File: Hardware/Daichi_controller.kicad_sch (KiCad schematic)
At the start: 24 parts, among them J1 USB_B_Mini, J2 S21, Q1 BF545A

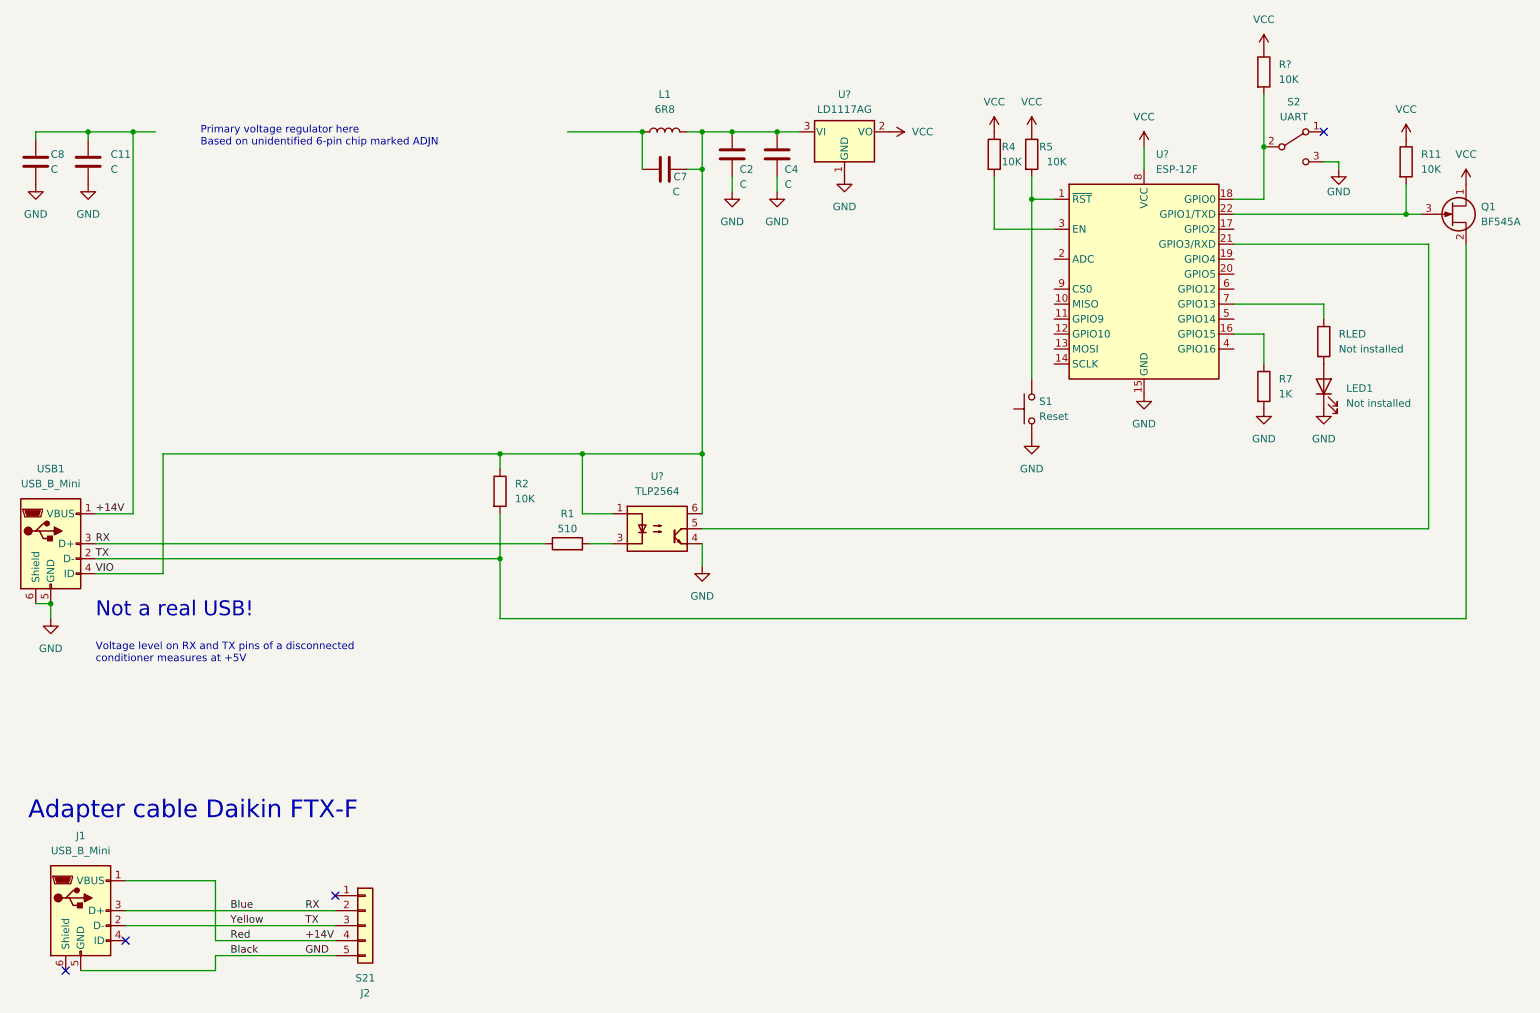
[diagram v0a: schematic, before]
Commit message: Hardware: Fix reference schematic
Q1 was drawn incorrectly. Thanks @glinka65 for hints
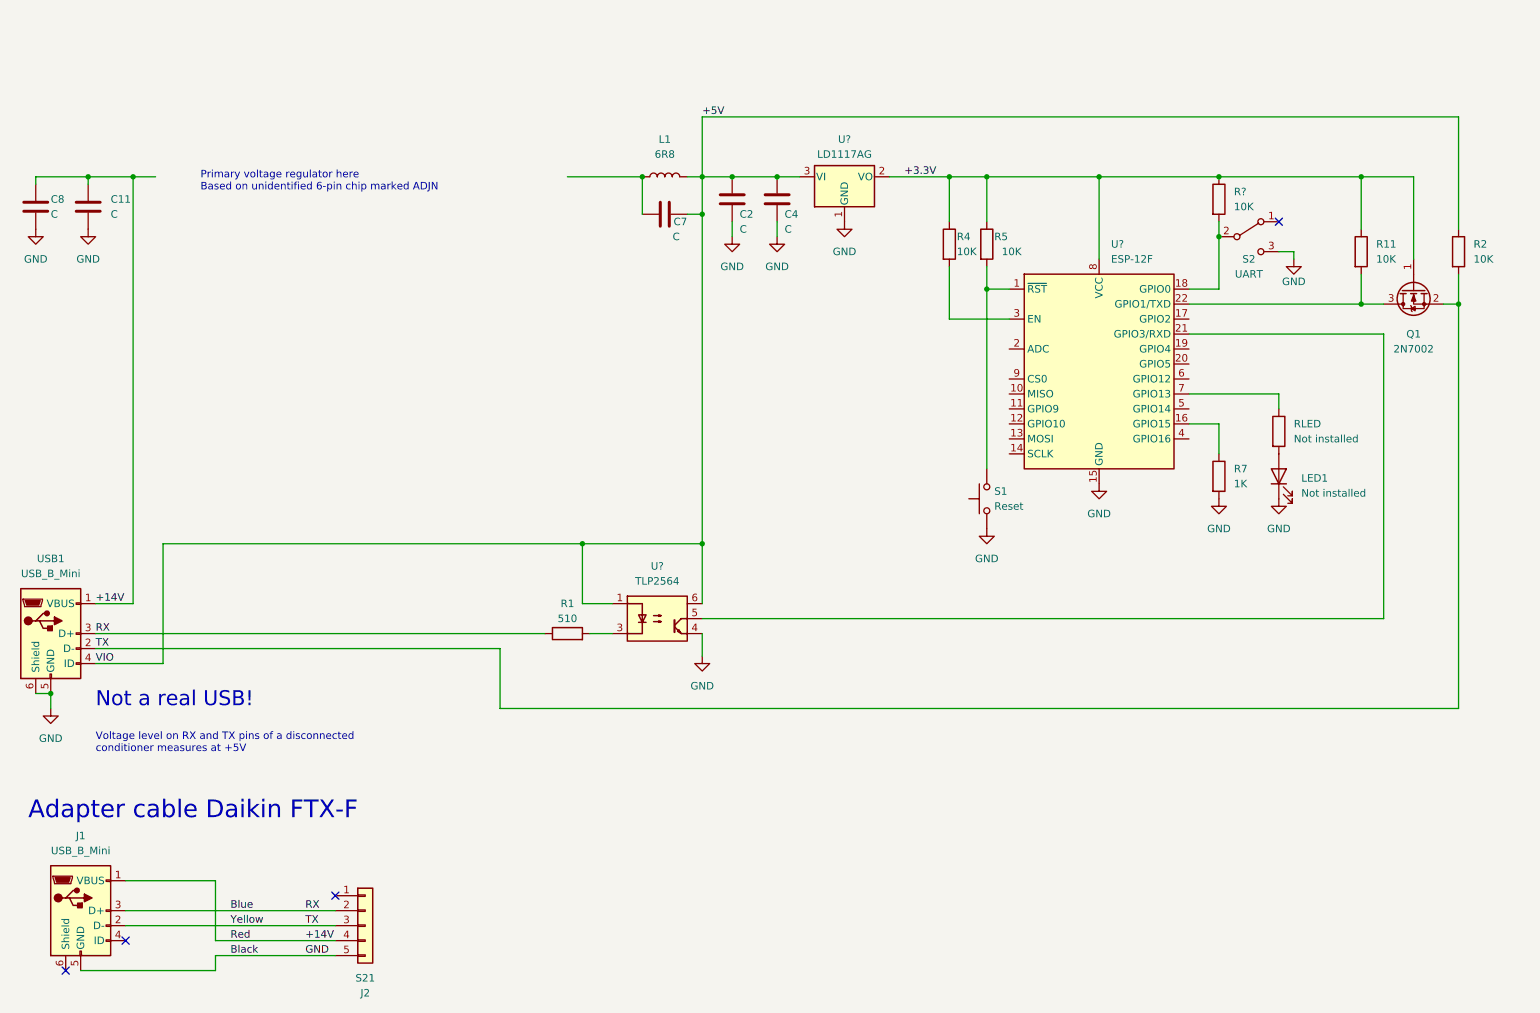
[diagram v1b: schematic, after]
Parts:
- removed Q1: BF545A, Package_TO_SOT_SMD:SOT-23, symbol Transistor_FET:BF545A
- added Q1: 2N7002, Package_TO_SOT_SMD:SOT-23, symbol Transistor_FET:2N7002
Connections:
- net TX: now also Q1.2 (S)
- net at R11.2, U?.22 (GPIO1/TXD): now also Q1.3 (D)
- net VCC renamed +3.3V
- net +3.3V: now also Q1.1 (G)
- net VIO renamed +5V
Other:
- moved on the sheet: C11, C2, C4, C7, C8, L1, LED1, R1, R11, R4, R5, R7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
